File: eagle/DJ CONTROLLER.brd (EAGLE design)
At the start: 101.6 x 53.3 mm, 91 parts, among them IC1 74HC4051, IC2 74HC4051, IC3 74HC4051, IC4 74HC4051

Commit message: Add files via upload
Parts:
- added JP79: (no value), pinhead:1X02
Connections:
- new net N$43: B1.RST, JP79.2
- net GND: now also JP79.1
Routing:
- net +5V: track 477.2 -> 532.0 mm
- net N$43: track 0.00 -> 47.6 mm
- net S0: track 218.2 -> 228.3 mm
- net N$1: track 8.89 -> 0.00 mm
- net S1: track 201.0 -> 206.1 mm
- net GND: track 578.5 -> 575.1 mm
- net FAD1: track 92.1 -> 93.3 mm
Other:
- board text added: "ASH DJ Controller"

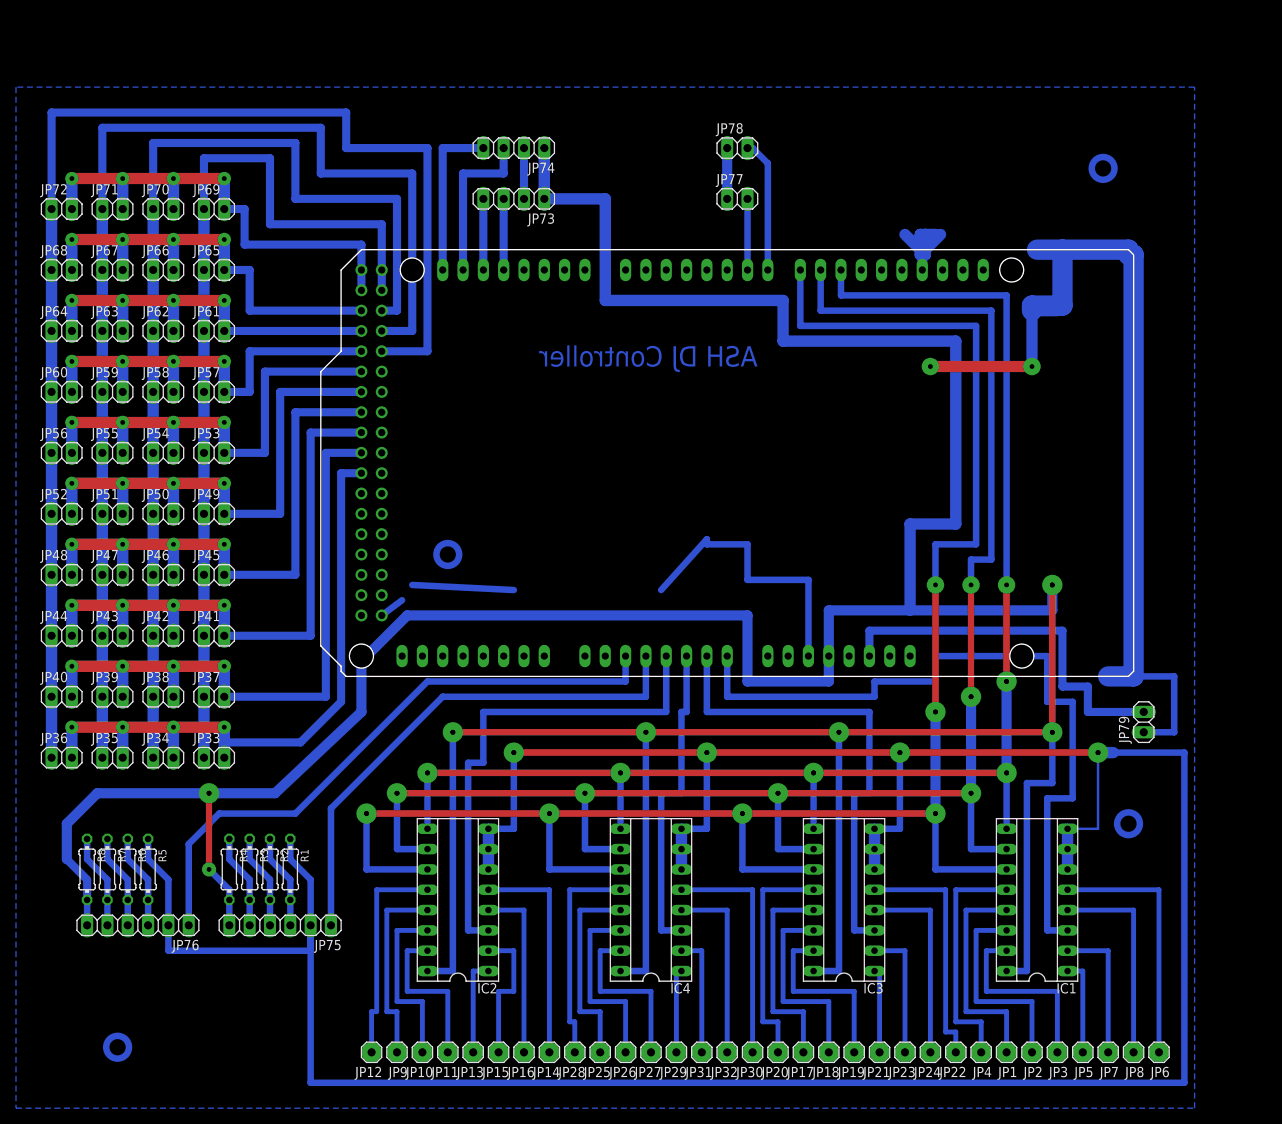
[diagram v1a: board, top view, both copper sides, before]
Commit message: added noise reduction capacitors for analog inputs
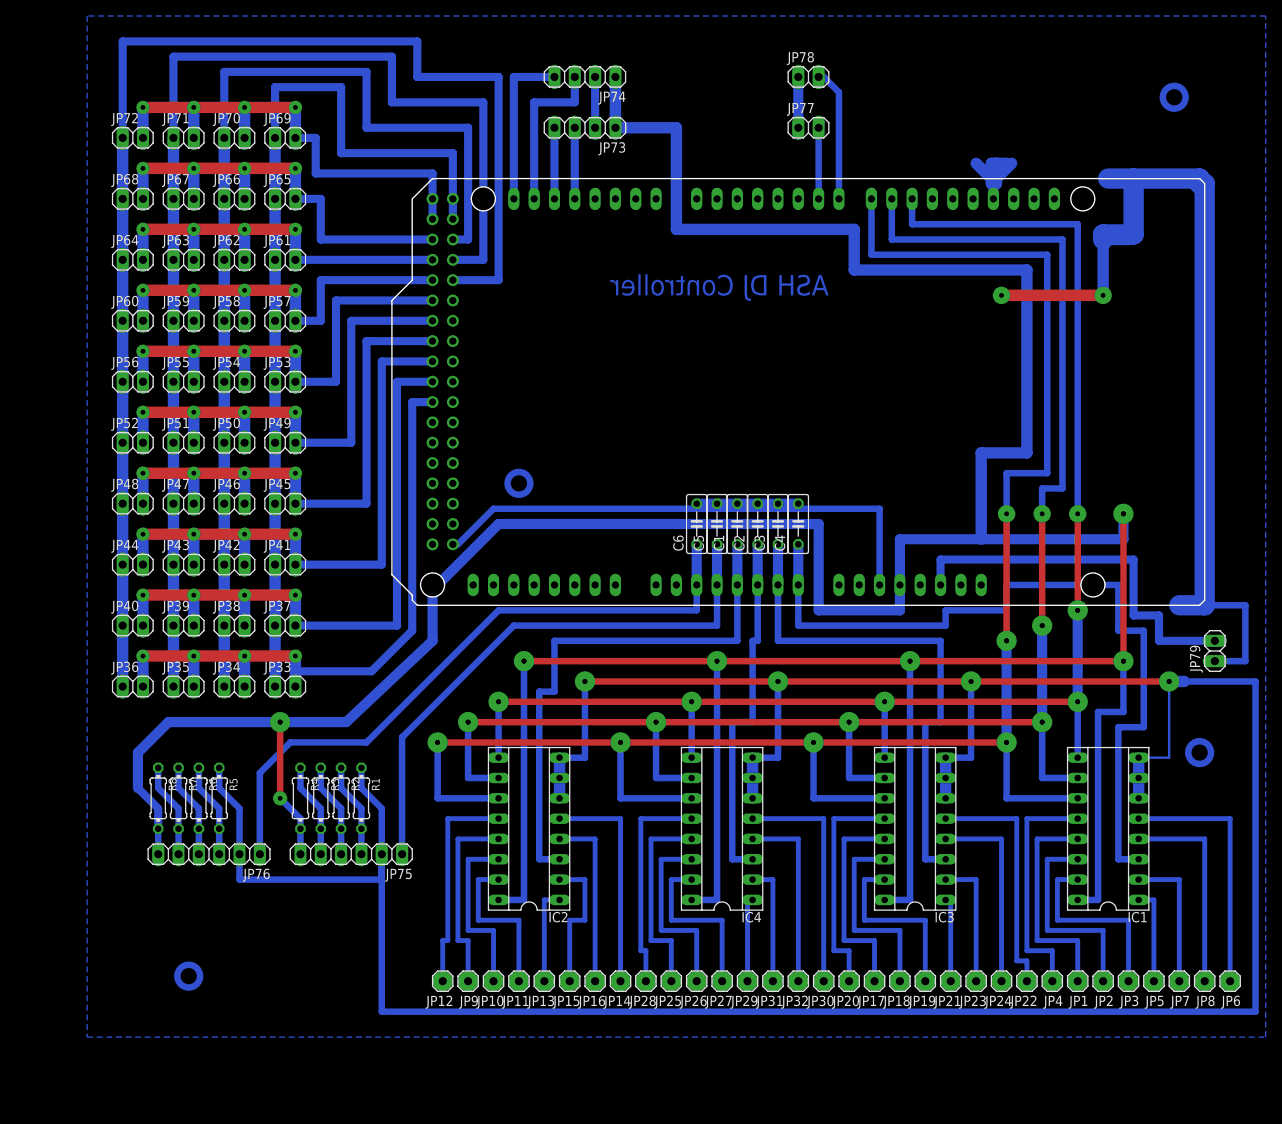
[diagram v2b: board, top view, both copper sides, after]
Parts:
- added C1, C2, C3, C4, C5, C6: (no value), resistor:C050-025X075
- moved B1 12.6 mm to (140.3, 54.6)
- moved IC1 12.6 mm to (128.3, 26.7)
- moved JP5 12.6 mm to (134.0, 7.62)
- moved JP8 12.6 mm to (140.3, 7.62)
- moved JP16 12.6 mm to (64.1, 7.62)
- moved IC2 12.6 mm to (55.9, 26.7)
- moved IC3 12.6 mm to (104.1, 26.7)
- moved IC4 12.6 mm to (80.0, 26.7)
- moved JP1 12.6 mm to (124.5, 7.62)
- moved JP10 12.6 mm to (51.4, 7.62)
- moved JP11 12.6 mm to (54.6, 7.62)
- moved JP12 12.6 mm to (45.1, 7.62)
- moved JP14 12.6 mm to (67.3, 7.62)
- moved JP15 12.6 mm to (61.0, 7.62)
- moved JP17 12.6 mm to (99.1, 7.62)
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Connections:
- net FAD1: now also C4.1
- net FAD2: now also C3.1
- net FAD3: now also C2.1
- net FAD4: now also C1.1
- net GND: now also C1.2, C2.2, C3.2, C4.2, C5.2, C6.2
- net MODE1: now also C5.1
- net MODE2: now also C6.1
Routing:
- net GND: track 575.1 -> 600.8 mm, vias 9 -> 10
- net FAD1: track 93.3 -> 98.4 mm
- net FAD4: track 61.6 -> 66.7 mm
- net MODE2: track 76.4 -> 81.4 mm
- net MODE1: track 64.8 -> 69.9 mm
- net FAD2: track 59.1 -> 64.1 mm
- net FAD3: track 40.0 -> 45.1 mm
- net +5V: track 532.0 -> 535.6 mm
